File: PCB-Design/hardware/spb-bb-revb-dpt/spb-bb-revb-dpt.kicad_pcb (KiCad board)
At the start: 4 copper layers, 89.5 x 85.2 mm, 201 parts, among them J1 DC+, J10 U.FL L2, J11 U.FL D2, J12 V_ISO,HS in: 1 +, 2 -, J13 V_ISO,LS in: 1 +, 2 -, J14 CTRL2: 1 RTN 2 PWMH 3 RTN 4 P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, J15 U.FL H3, J16 U.FL L3, J17 U.FL D3, J18 U.FL H4, J19 U.FL L4, J2 DC-, J20 U.FL D4, J21 AC, J3 V_ISO,HS in: 1 +, 2 -, J4 V_ISO,LS in: 1 +, 2 -, J5 CTRL1: 1 RTN 2 PWMH 3 RTN 4 P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, J6 U.FL H1, J7 U.FL L1, J8 U.FL D1, J9 U.FL H2, Q1 EPC2361, Q2 EPC2361, Q3 EPC2361, Q4 EPC2361, Q5 EPC2361, Q6 EPC2361, Q7 EPC2361, Q8 EPC2361, U1 2EDF7275K, U2 2EDF7275K

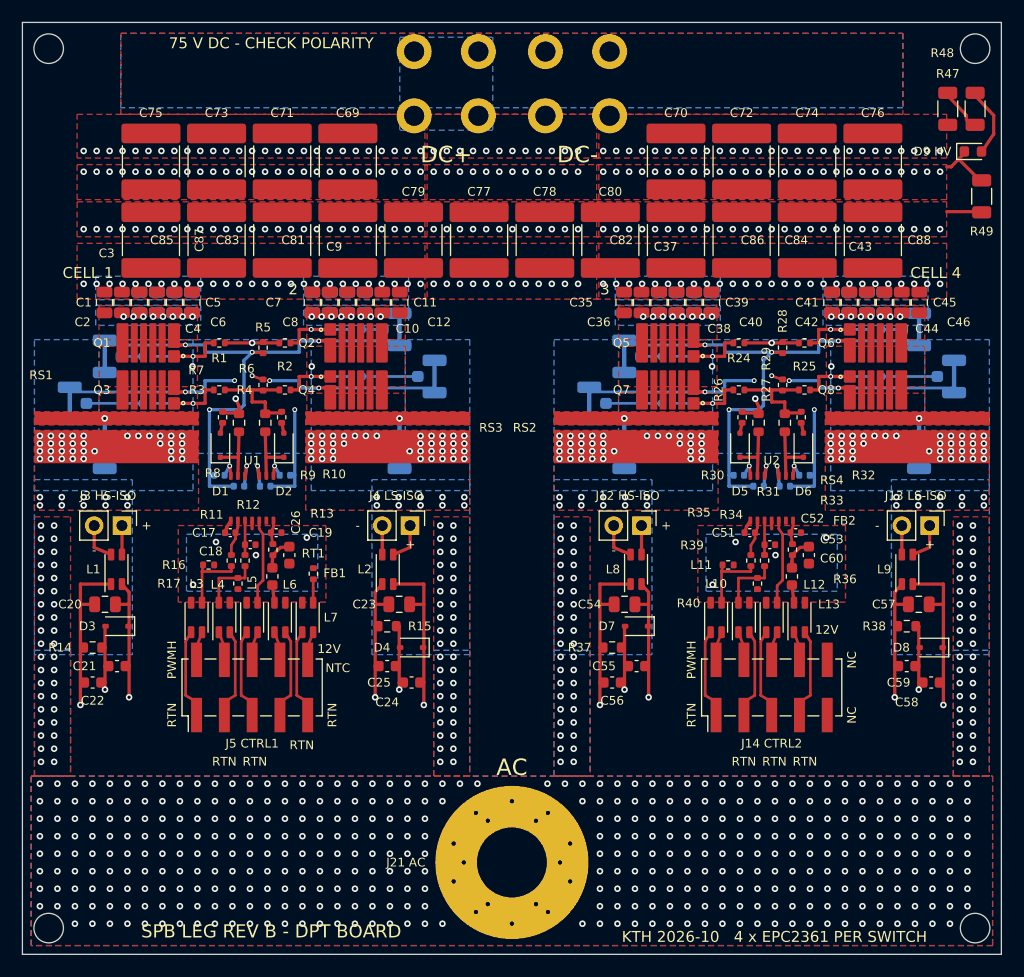
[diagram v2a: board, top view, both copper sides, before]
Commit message: Rev B boards: 0.5 mm bare-pad rule for the 75 V nets, all 0402 parts to 0603
- New DRC rule: bare pads of different power nets >= 0.5 mm on the outer layers
  (IPC-2221B A6), EPC2361 land pattern and shunt IN land excepted. Bank row A 0.25 mm
  up (was 0.30 mm to row B), top bypass row 0.1 mm towards the bank (0.45 mm to the
  HS gate pads).
- All 0402 resistors/capacitors (and the NTC) are now 0603 for hand soldering; driver
  input side, R_OFF/diode, bottom-side decoupling and U.FL resistors re-placed.
  External PWM pull-downs and the 12 V 4.7 uF dropped (internal 150 k pull-downs;
  12 V only feeds VDDI through 3 k).
- DRC 0/0 and schematic = PCB on both boards; fab outputs and renders regenerated.

Co-Authored-By: Claude Opus 5.5 <noreply@anthropic.com>
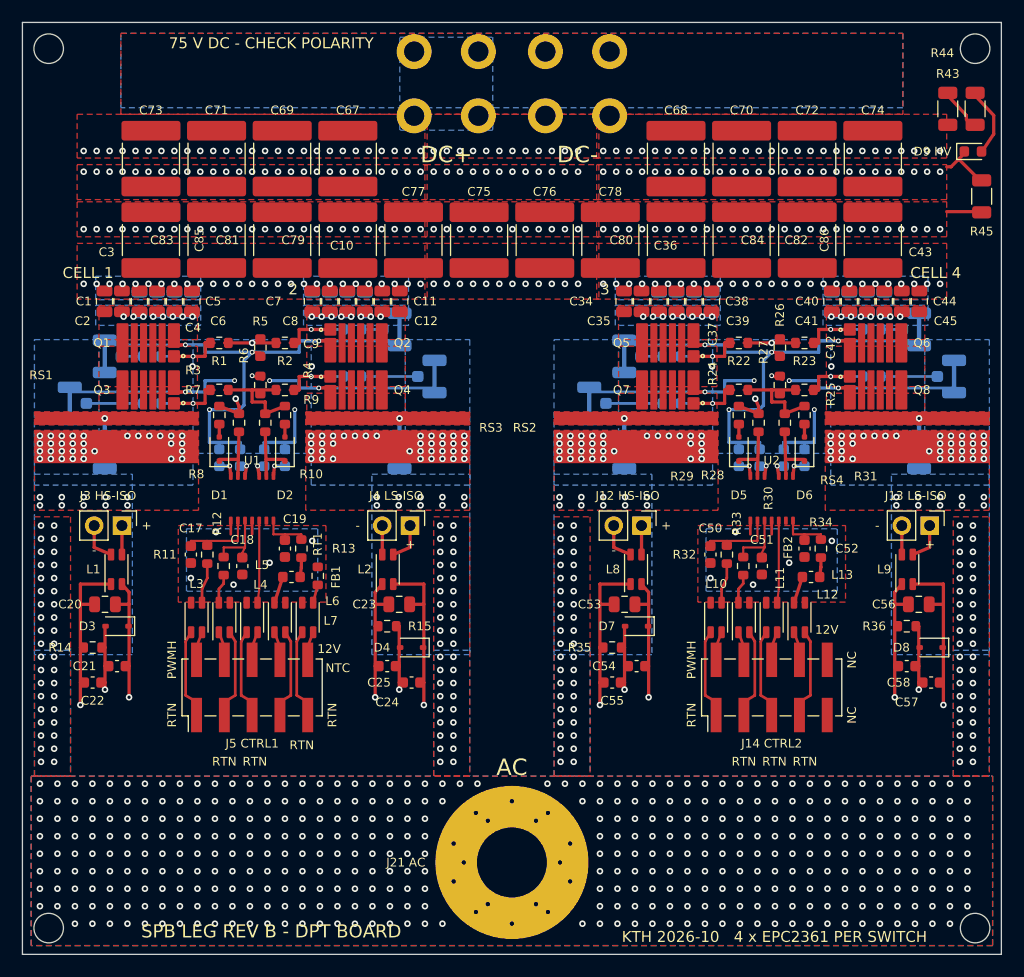
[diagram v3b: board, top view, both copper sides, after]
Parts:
- removed C87, C88: 22uF 100V X7S 2220, spb_fab:C_2220_5750Metric_TightCrtYd
- removed R46: 953R 1% (V_DS LS, 20:1 into 50 R), Resistor_SMD:R_0402_1005Metric
- removed R47, R48: 68k 1206 (HV LED), Resistor_SMD:R_1206_3216Metric
- removed R49: 100k 1206 (bleeder), Resistor_SMD:R_1206_3216Metric
- C13, C14, C15, C16, C47, C48, C49: value 1uF 16V X7R 0402 -> 1uF 16V X7R 0603; footprint Capacitor_SMD:C_0402_1005Metric -> Capacitor_SMD:C_0603_1608Metric
- C17, C18, C51: value 100pF C0G 0402 -> 100pF C0G 0603; footprint Capacitor_SMD:C_0402_1005Metric -> Capacitor_SMD:C_0603_1608Metric
- C19: value 22nF 25V X7R 0402 -> 22nF 25V X7R 0603; footprint Capacitor_SMD:C_0402_1005Metric -> Capacitor_SMD:C_0603_1608Metric
- C26, C60: value 4.7uF 25V X5R 0603 (12 V) -> 1uF 100V X7S; footprint Capacitor_SMD:C_0603_1608Metric -> spb_fab:C_0805_2012Metric_TightCrtYd; moved to B.Cu
- C34: moved to F.Cu
- C46: value 1uF 100V X7S -> 1uF 16V X7R 0603; footprint spb_fab:C_0805_2012Metric_TightCrtYd -> Capacitor_SMD:C_0603_1608Metric; moved to B.Cu
- C50: value 1uF 16V X7R 0402 -> 100pF C0G 0603; footprint Capacitor_SMD:C_0402_1005Metric -> Capacitor_SMD:C_0603_1608Metric; moved to F.Cu
- C52: value 100pF C0G 0402 -> 22nF 25V X7R 0603; footprint Capacitor_SMD:C_0402_1005Metric -> Capacitor_SMD:C_0603_1608Metric
- C53: value 22nF 25V X7R 0402 -> 4.7uF 25V X7R 0805; footprint Capacitor_SMD:C_0402_1005Metric -> Capacitor_SMD:C_0805_2012Metric
- C54, C57: value 4.7uF 25V X7R 0805 -> 4.7uF 16V X5R 0603; footprint Capacitor_SMD:C_0805_2012Metric -> Capacitor_SMD:C_0603_1608Metric
- C56: value 4.7uF 16V X5R 0603 -> 4.7uF 25V X7R 0805; footprint Capacitor_SMD:C_0603_1608Metric -> Capacitor_SMD:C_0805_2012Metric
- C59: value 4.7uF 16V X5R 0603 -> 1uF 100V X7S; footprint Capacitor_SMD:C_0603_1608Metric -> spb_fab:C_0805_2012Metric_TightCrtYd; moved to B.Cu
- C67, C68: value 1uF 100V X7S -> 22uF 100V X7S 2220; footprint spb_fab:C_0805_2012Metric_TightCrtYd -> spb_fab:C_2220_5750Metric_TightCrtYd; moved to F.Cu
- R1, R10, R11, R12, R13, R2, R3, R4, R5, R6, R8: footprint Resistor_SMD:R_0402_1005Metric -> Resistor_SMD:R_0603_1608Metric
- R16: value 10k (PWM_H pull-down) -> 0R (V_GS HS); footprint Resistor_SMD:R_0402_1005Metric -> Resistor_SMD:R_0603_1608Metric; moved to B.Cu
- R17: value 10k (PWM_L pull-down) -> 0R (V_GS LS); footprint Resistor_SMD:R_0402_1005Metric -> Resistor_SMD:R_0603_1608Metric; moved to B.Cu
- R18, R21: value 0R (V_GS HS) -> 953R 1% (V_DS LS, 20:1 into 50 R); footprint Resistor_SMD:R_0402_1005Metric -> Resistor_SMD:R_0603_1608Metric
- R19: value 0R (V_GS LS) -> 0R (V_GS HS); footprint Resistor_SMD:R_0402_1005Metric -> Resistor_SMD:R_0603_1608Metric
- R20: value 953R 1% (V_DS LS, 20:1 into 50 R) -> 0R (V_GS LS); footprint Resistor_SMD:R_0402_1005Metric -> Resistor_SMD:R_0603_1608Metric
- R22: value 0R (V_GS LS) -> 0R5 1% (R_G HL); footprint Resistor_SMD:R_0402_1005Metric -> Resistor_SMD:R_0603_1608Metric; moved to F.Cu
- R23: value 953R 1% (V_DS LS, 20:1 into 50 R) -> 0R5 1% (R_G HR); footprint Resistor_SMD:R_0402_1005Metric -> Resistor_SMD:R_0603_1608Metric; moved to F.Cu
- R24: value 0R5 1% (R_G HL) -> 0R5 1% (R_G LL); footprint Resistor_SMD:R_0402_1005Metric -> Resistor_SMD:R_0603_1608Metric
- R25: value 0R5 1% (R_G HR) -> 0R5 1% (R_G LR); footprint Resistor_SMD:R_0402_1005Metric -> Resistor_SMD:R_0603_1608Metric
- R26: value 0R5 1% (R_G LL) -> 10k 1% (HS gate pull-down); footprint Resistor_SMD:R_0402_1005Metric -> Resistor_SMD:R_0603_1608Metric
- R27: value 0R5 1% (R_G LR) -> 10k 1% (LS gate pull-down); footprint Resistor_SMD:R_0402_1005Metric -> Resistor_SMD:R_0603_1608Metric
- R28: value 10k 1% (HS gate pull-down) -> 0R75 1% (R_ON,A); footprint Resistor_SMD:R_0402_1005Metric -> Resistor_SMD:R_0603_1608Metric
- R29: value 10k 1% (LS gate pull-down) -> 0R (R_OFF,A); footprint Resistor_SMD:R_0402_1005Metric -> Resistor_SMD:R_0603_1608Metric
- R30: value 0R75 1% (R_ON,A) -> 0R75 1% (R_ON,B)
- R31: value 0R (R_OFF,A) -> 0R (R_OFF,B); footprint Resistor_SMD:R_0402_1005Metric -> Resistor_SMD:R_0603_1608Metric
- R32: value 0R75 1% (R_ON,B) -> 47R 1% (INA)
- R33: value 0R (R_OFF,B) -> 47R 1% (INB); footprint Resistor_SMD:R_0402_1005Metric -> Resistor_SMD:R_0603_1608Metric
- R34: value 47R 1% (INA) -> 3k 1% (RVDDI); footprint Resistor_SMD:R_0402_1005Metric -> Resistor_SMD:R_0603_1608Metric
- R35: value 47R 1% (INB) -> 150R 1% 0603 (bias, <= 82 mW); footprint Resistor_SMD:R_0402_1005Metric -> Resistor_SMD:R_0603_1608Metric
- R36: value 3k 1% (RVDDI) -> 150R 1% 0603 (bias, <= 82 mW); footprint Resistor_SMD:R_0402_1005Metric -> Resistor_SMD:R_0603_1608Metric
- R37: value 150R 1% 0603 (bias, <= 82 mW) -> 0R (V_GS HS); moved to B.Cu
- R38: value 150R 1% 0603 (bias, <= 82 mW) -> 0R (V_GS LS); moved to B.Cu
- R39: value 10k (PWM_H pull-down) -> 953R 1% (V_DS LS, 20:1 into 50 R); footprint Resistor_SMD:R_0402_1005Metric -> Resistor_SMD:R_0603_1608Metric; moved to B.Cu
- R40: value 10k (PWM_L pull-down) -> 0R (V_GS HS); footprint Resistor_SMD:R_0402_1005Metric -> Resistor_SMD:R_0603_1608Metric; moved to B.Cu
- R41: value 0R (V_GS HS) -> 0R (V_GS LS); footprint Resistor_SMD:R_0402_1005Metric -> Resistor_SMD:R_0603_1608Metric
- R42: value 0R (V_GS LS) -> 953R 1% (V_DS LS, 20:1 into 50 R); footprint Resistor_SMD:R_0402_1005Metric -> Resistor_SMD:R_0603_1608Metric
- R43: value 953R 1% (V_DS LS, 20:1 into 50 R) -> 68k 1206 (HV LED); footprint Resistor_SMD:R_0402_1005Metric -> Resistor_SMD:R_1206_3216Metric; moved to F.Cu
- R44: value 0R (V_GS HS) -> 68k 1206 (HV LED); footprint Resistor_SMD:R_0402_1005Metric -> Resistor_SMD:R_1206_3216Metric; moved to F.Cu
- R45: value 0R (V_GS LS) -> 100k 1206 (bleeder); footprint Resistor_SMD:R_0402_1005Metric -> Resistor_SMD:R_1206_3216Metric; moved to F.Cu
- RT1: value NTC 10k B3380 -> NTC 10k B3380 0603; footprint Resistor_SMD:R_0402_1005Metric -> Resistor_SMD:R_0603_1608Metric
- moved C67 47.7 mm to (135.0, 88.0), turned to 90 degrees
- moved C59 42.7 mm to (163.4, 101.2), turned to -90 degrees
- moved R23 42.1 mm to (176.8, 104.9)
- moved R43 40.6 mm to (189.8, 83.5), turned to 90 degrees
- moved R22 35.0 mm to (170.8, 104.9)
- moved C75 30.9 mm to (147.0, 95.5)
- moved C76 30.9 mm to (153.0, 95.5)
- moved R38 29.7 mm to (164.6, 110.4)
- moved C56 28.9 mm to (187.2, 128.8)
- moved C34 28.5 mm to (160.2, 101.1), turned to 90 degrees
- moved R37 27.2 mm to (164.6, 106.1)
- moved C26 26.9 mm to (116.0, 101.2), turned to -90 degrees
- moved C60 26.1 mm to (165.1, 101.2), turned to -90 degrees
- moved R40 25.5 mm to (182.9, 103.7), turned to 0 degrees
- moved R44 22.1 mm to (192.3, 83.5), turned to 90 degrees
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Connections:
- C15 pad 1: VEEB1 -> KL1
- C15 pad 2: KL1 -> VEEB1
- C16 pad 1: VDDB1 -> KL1
- C16 pad 2: KL1 -> VDDB1
- C18 pad 1: INB1 -> GNDI1
- C18 pad 2: GNDI1 -> INB1
- C19 pad 1: VDDI1 -> GNDI1
- C19 pad 2: GNDI1 -> VDDI1
- C26 pad 1: GNDI1 -> DCN
- C26 pad 2: +12V1 -> DCP
- C34 pad 1: DCN -> DCP
- C34 pad 2: DCP -> DCN
- C46 pad 1: DCP -> KH2
- C46 pad 2: DCN -> VDDA2
- C47 pad 2: VDDA2 -> VEEA2
- C48 pad 1: KH2 -> KL2
- C48 pad 2: VEEA2 -> VEEB2
- C49 pad 1: VEEB2 -> KL2
- C49 pad 2: KL2 -> VDDB2
- C50 pad 1: VDDB2 -> GNDI2
- C50 pad 2: KL2 -> INA2
- C51 pad 2: INA2 -> INB2
- C52 pad 1: INB2 -> GNDI2
- C52 pad 2: GNDI2 -> VDDI2
- C53 pad 1: VDDI2 -> VEEA2
- C53 pad 2: GNDI2 -> VDDA2
- C54 pad 1: VEEA2 -> KH2
- C55 pad 1: KH2 -> VEEA2
- C55 pad 2: VDDA2 -> KH2
- C56 pad 1: VEEA2 -> VEEB2
- C56 pad 2: KH2 -> VDDB2
- C57 pad 2: VDDB2 -> KL2
- C58 pad 1: VEEB2 -> KL2
- C58 pad 2: KL2 -> VDDB2
- C59 pad 1: KL2 -> DCN
- C59 pad 2: VDDB2 -> DCP
- C60 pad 1: GNDI2 -> DCN
- C60 pad 2: +12V2 -> DCP
- R16 pad 1: PWM_H1 -> UFL_H1
- R16 pad 2: GNDI1 -> GH_L1
- R17 pad 1: GNDI1 -> UFL_L1
- R17 pad 2: PWM_L1 -> GL_L1
- R18 pad 1: UFL_H1 -> UFL_D1
- R18 pad 2: GH_L1 -> SW
- R19 pad 1: UFL_L1 -> GH_R1
- R19 pad 2: GL_L1 -> UFL_H2
- R20 pad 1: UFL_D1 -> GL_R1
- R20 pad 2: SW -> UFL_L2
- R21 pad 1: GH_R1 -> SW
- R21 pad 2: UFL_H2 -> UFL_D2
- R22 pad 1: GL_R1 -> GH_L2
- R22 pad 2: UFL_L2 -> GH_STAR2
- R23 pad 1: SW -> GH_STAR2
- R23 pad 2: UFL_D2 -> GH_R2
- R24 pad 1: GH_L2 -> GL_L2
- R24 pad 2: GH_STAR2 -> GL_STAR2
- R25 pad 1: GH_STAR2 -> GL_STAR2
- R25 pad 2: GH_R2 -> GL_R2
- R26 pad 1: GL_L2 -> KH2
- R26 pad 2: GL_STAR2 -> GH_STAR2
- R27 pad 2: GL_R2 -> KL2
- R28 pad 1: KH2 -> OUTA2
- R29 pad 1: GL_STAR2 -> OFFA2
- R29 pad 2: KL2 -> GH_STAR2
- R30 pad 1: OUTA2 -> OUTB2
- R30 pad 2: GH_STAR2 -> GL_STAR2
- R31 pad 1: OFFA2 -> OFFB2
- R31 pad 2: GH_STAR2 -> GL_STAR2
- R32 pad 1: OUTB2 -> PWM_H2
- R32 pad 2: GL_STAR2 -> INA2
- R33 pad 1: OFFB2 -> PWM_L2
- R33 pad 2: GL_STAR2 -> INB2
- R34 pad 1: PWM_H2 -> +12V2
- R34 pad 2: INA2 -> VDDI2
- R35 pad 1: PWM_L2 -> VEEA2
- R35 pad 2: INB2 -> KH2
- R36 pad 1: +12V2 -> VEEB2
- R36 pad 2: VDDI2 -> KL2
- R37 pad 1: VEEA2 -> UFL_H3
- R37 pad 2: KH2 -> GH_L2
- R38 pad 1: VEEB2 -> UFL_L3
- R38 pad 2: KL2 -> GL_L2
- R39 pad 1: PWM_H2 -> UFL_D3
- R39 pad 2: GNDI2 -> SW
- R40 pad 1: GNDI2 -> GH_R2
- R40 pad 2: PWM_L2 -> UFL_H4
- R41 pad 1: UFL_H3 -> GL_R2
- R41 pad 2: GH_L2 -> UFL_L4
- R42 pad 1: UFL_L3 -> SW
- R42 pad 2: GL_L2 -> UFL_D4
- R43 pad 1: UFL_D3 -> DCP
- R43 pad 2: SW -> HVA
- R44 pad 1: GH_R2 -> HVA
- R44 pad 2: UFL_H4 -> HVB
- R45 pad 1: GL_R2 -> DCP
- R45 pad 2: UFL_L4 -> DCN
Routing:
- net INA1: track 3.33 -> 7.05 mm
- net INA2: track 3.33 -> 7.05 mm
- net INB1: track 3.17 -> 6.26 mm
- net INB2: track 3.17 -> 6.26 mm
- net PWM_L1: track 5.76 -> 2.69 mm
- net PWM_L2: track 5.76 -> 2.69 mm
- net PWM_H1: track 6.66 -> 3.68 mm
- net PWM_H2: track 6.66 -> 3.68 mm
- net KL2: track 102.5 -> 99.9 mm
- net KL1: track 102.5 -> 99.9 mm
- net KH2: track 97.8 -> 95.2 mm
- net KH1: track 97.8 -> 95.2 mm
- net VDDI2: track 2.23 -> 4.80 mm
- net VDDI1: track 2.23 -> 4.80 mm
- net VEEA2: track 55.6 -> 54.4 mm
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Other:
- board text removed: "C87"
- board text removed: "C88"
- board text removed: "R46"
- board text removed: "R47"
- board text removed: "R48"
- board text removed: "R49"

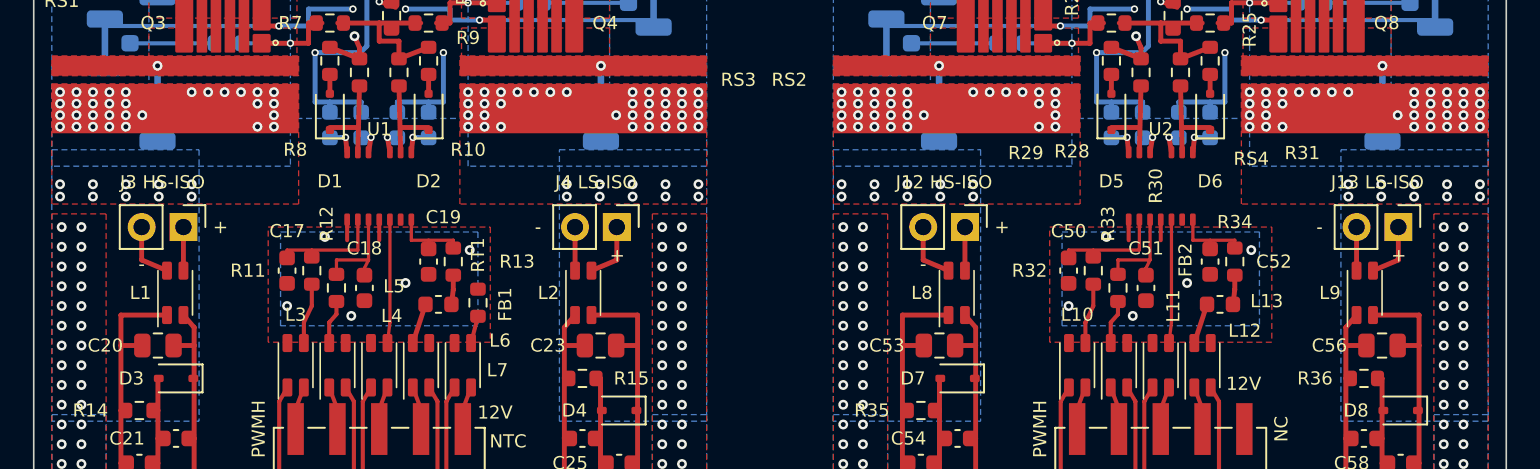
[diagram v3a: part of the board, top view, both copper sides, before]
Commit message: Rev B boards: V_DS port as a 4.99 k 2512 divider (100:1 into 50 R)
- R18/R21/R39/R42: 4.99 k 1 % 2512 (Vishay CRCW25124K99FKEGHP, 1.5 W);
  1.1 W at 75 V into the 50 R scope input, ~0.75 V at the U.FL, so the
  V_DS U.FL is back to U.FL-R-SMT-1(10).
- 2512 on the bottom SW pour under the AC column; 50 R side routed to the
  U.FL through the DC- via-row gap.
- Schematic note and PCB rules document updated.
- DRC 0/0 and schematic = PCB on both boards; fab outputs and renders
  regenerated.

Co-Authored-By: Claude Opus 5.5 <noreply@anthropic.com>
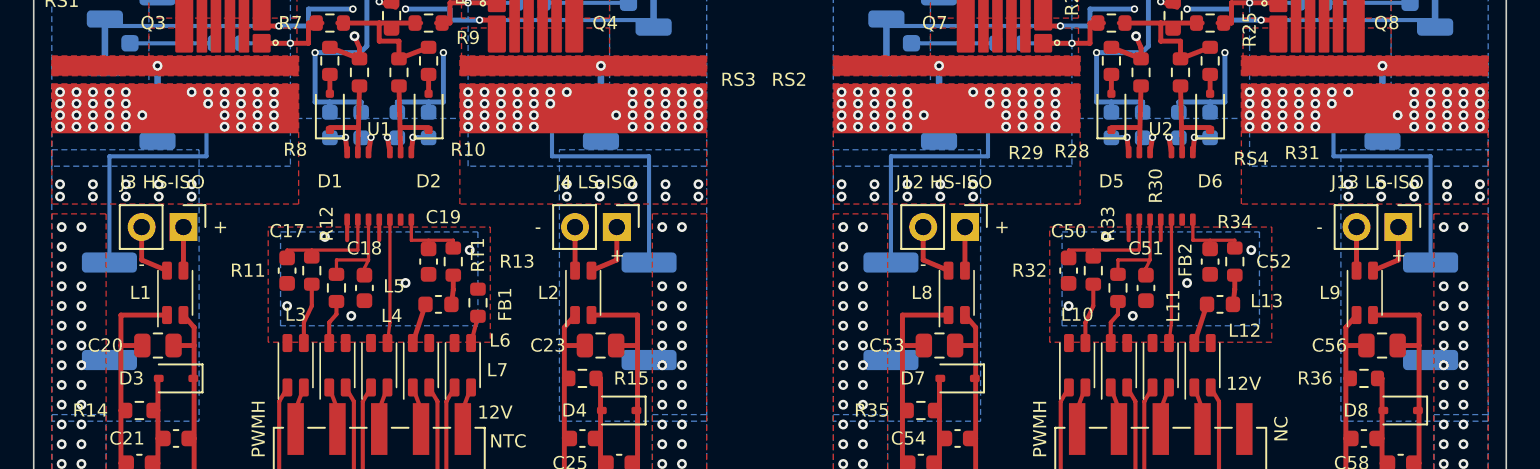
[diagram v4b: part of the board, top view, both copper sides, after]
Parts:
- R18, R21, R39, R42: value 953R 1% (V_DS LS, 20:1 into 50 R) -> 4.99k 1% 2512 (V_DS LS, 100:1 into 50 R); footprint Resistor_SMD:R_0603_1608Metric -> Resistor_SMD:R_2512_6332Metric
- moved R21 13.8 mm to (142.7, 126.7), turned to -90 degrees
- moved R39 13.8 mm to (157.3, 126.7), turned to -90 degrees
- moved R42 13.8 mm to (190.2, 126.7), turned to -90 degrees
- moved R18 13.8 mm to (109.8, 126.7), turned to -90 degrees
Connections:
- J1 pad : (no net) -> DCP
- J2 pad : (no net) -> DCN
- R21 pad 1: SW -> UFL_D2
- R21 pad 2: UFL_D2 -> SW
- R42 pad 1: SW -> UFL_D4
- R42 pad 2: UFL_D4 -> SW
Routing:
- net UFL_D4: track 1.92 -> 16.2 mm
- net UFL_D3: track 1.92 -> 16.2 mm
- net UFL_D2: track 1.92 -> 16.2 mm
- net UFL_D1: track 1.92 -> 16.2 mm
- net SW: vias 568 -> 556
- net DCN: vias 308 -> 340
